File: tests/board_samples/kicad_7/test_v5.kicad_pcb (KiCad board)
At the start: 2 copper layers, 4 parts

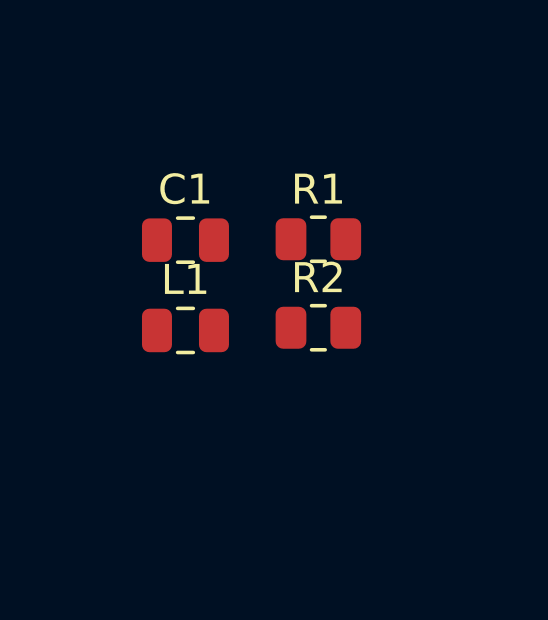
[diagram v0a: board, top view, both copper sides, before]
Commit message: [Tests][Makefile][Fixed] Missing 3D model in test_v5.kicad_pcb
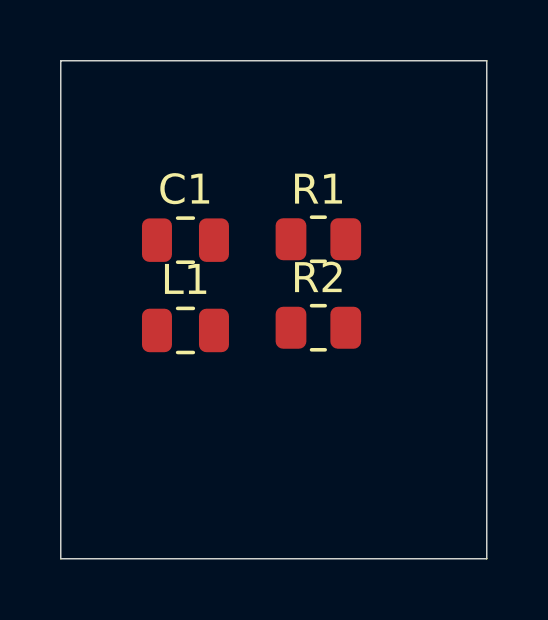
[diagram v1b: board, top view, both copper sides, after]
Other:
- board outline added: 14.2 x 16.6 mm
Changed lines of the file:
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@@
     )
   )
-  (property "VAL_C2" "1000 pF")
-  (property "text" "Test")
   (net 0 "")
   (net 1 "unconnected-(C1-Pad1)")
@@
       (rotate (xyz 0 0 0))
     )
-  )
+    (model "${KIPRJMOD}/../../data/R_0805_2012Metric.wrl"
+      (offset (xyz 0 0 0))
+      (scale (xyz 1 1 1))
+      (rotate (xyz 0 0 0))
+    )
+ )
+  (gr_rect (start 126.7 71.3) (end 140.9 87.9)
+    (stroke (width 0.05) (type default)) (fill none) (layer "Edge.Cuts"))
 )
